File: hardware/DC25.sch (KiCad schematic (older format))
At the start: 18 parts, among them P2 CONN_01X04, SW1 SW_DPDT_x2, U1 ATMEGA328P-AU, Y1 16MHz

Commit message: Some progress
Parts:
- DIS1: footprint footprints:VFD -> (none)
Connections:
- net DB0: now also U1.14 ((PCINT2/OC1B/~SS~)PB2); no longer U1.1 ((PCINT19/OC2B/INT1)PD3)
- net DB1: now also U1.13 ((PCINT1/OC1A)PB1); no longer U1.2 ((PCINT20/XCK/T0)PD4)
- net DB2: now also U1.12 ((PCINT0/CLKO/ICP1)PB0); no longer U1.9 ((PCINT21/OC0B/T1)PD5)
- net DB3: now also U1.11 ((PCINT23/AIN1)PD7); no longer U1.10 ((PCINT22/OC0A/AIN0)PD6)
- net DB4: now also U1.10 ((PCINT22/OC0A/AIN0)PD6); no longer U1.11 ((PCINT23/AIN1)PD7)
- net DB5: now also U1.9 ((PCINT21/OC0B/T1)PD5); no longer U1.12 ((PCINT0/CLKO/ICP1)PB0)
- net DB6: now also U1.2 ((PCINT20/XCK/T0)PD4); no longer U1.13 ((PCINT1/OC1A)PB1)
- net DB7: now also U1.1 ((PCINT19/OC2B/INT1)PD3); no longer U1.14 ((PCINT2/OC1B/~SS~)PB2)
- net E: now also U1.23 ((PCINT8/ADC0)PC0); no longer U1.32 ((PCINT18/INT0)PD2)
- net RGB1: now also U1.30 ((PCINT16/RXD)PD0); no longer U1.23 ((PCINT8/ADC0)PC0)
- net RS: now also U1.25 ((PCINT10/ADC2)PC2); no longer U1.30 ((PCINT16/RXD)PD0)
- net RW: now also U1.24 ((PCINT9/ADC1)PC1); no longer U1.31 ((PCINT17/TXD)PD1)
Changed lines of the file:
@@
 	-1   0    0    1
-$EndComp
-$Comp
-L VFD DIS1
-U 1 1 58C89F6D
-P 3950 850
-F 0 "DIS1" H 4450 900 60  0000 C CNN
-F 1 "VFD" H 3400 900 60  0000 C CNN
-F 2 "footprints:VFD" H 3500 950 60  0001 C CNN
-F 3 "" H 3500 950 60  0001 C CNN
-	1    3950 850
-	1    0    0    -1
 $EndComp
 NoConn ~ 3500 1250
@@
 Text Label 4600 1250 3    60   ~ 0
 DB7
-Text Label 2850 2400 0    60   ~ 0
+Text Label 2850 1850 0    60   ~ 0
 RS
-Text Label 2850 2500 0    60   ~ 0
+Text Label 2850 1750 0    60   ~ 0
 RW
+Text Label 2850 1000 0    60   ~ 0
+DB0
+Text Label 2850 900  0    60   ~ 0
+DB1
+Text Label 2850 800  0    60   ~ 0
+DB2
+Text Label 2850 3100 0    60   ~ 0
+DB3
+Text Label 2850 3000 0    60   ~ 0
+DB4
+Text Label 2850 2900 0    60   ~ 0
+DB5
+Text Label 2850 2800 0    60   ~ 0
+DB6
 Text Label 2850 2700 0    60   ~ 0
-DB0
-Text Label 2850 2800 0    60   ~ 0
-DB1
-Text Label 2850 2900 0    60   ~ 0
-DB2
-Text Label 2850 3000 0    60   ~ 0
-DB3
-Text Label 2850 3100 0    60   ~ 0
-DB4
-Text Label 2850 800  0    60   ~ 0
-DB5
-Text Label 2850 900  0    60   ~ 0
-DB6
-Text Label 2850 1000 0    60   ~ 0
 DB7
 $Comp
@@
 Text Label 10300 5100 0    60   ~ 0
 RGB1
-Text Label 2850 1650 0    60   ~ 0
+Text Label 2850 2400 0    60   ~ 0
 RGB1
-NoConn ~ 2850 1750
-NoConn ~ 2850 1850
+NoConn ~ 2850 2500
+NoConn ~ 2850 2500
 NoConn ~ 2850 1950
 NoConn ~ 2850 2050
@@
 Wire Wire Line
 	850  3000 950  3000
-Text Label 2850 2600 0    60   ~ 0
+Text Label 2850 1650 0    60   ~ 0
 E
 NoConn ~ 2850 2150
@@
 	950  900  800  900
 Connection ~ 800  900
+$Comp
+L VFD DIS1
+U 1 1 58D4713E
+P 3950 850
+F 0 "DIS1" H 4450 900 60  0000 C CNN
+F 1 "VFD" H 3400 900 60  0000 C CNN
+F 2 "" H 3500 950 60  0001 C CNN
+F 3 "" H 3500 950 60  0001 C CNN
+	1    3950 850
+	1    0    0    -1
+$EndComp
 $EndSCHEMATC

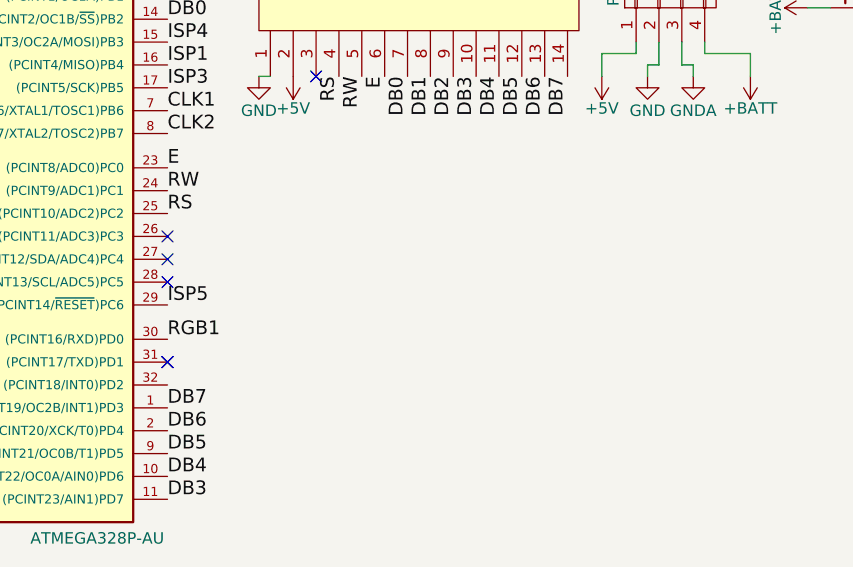
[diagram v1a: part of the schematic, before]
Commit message: Finish board layout.
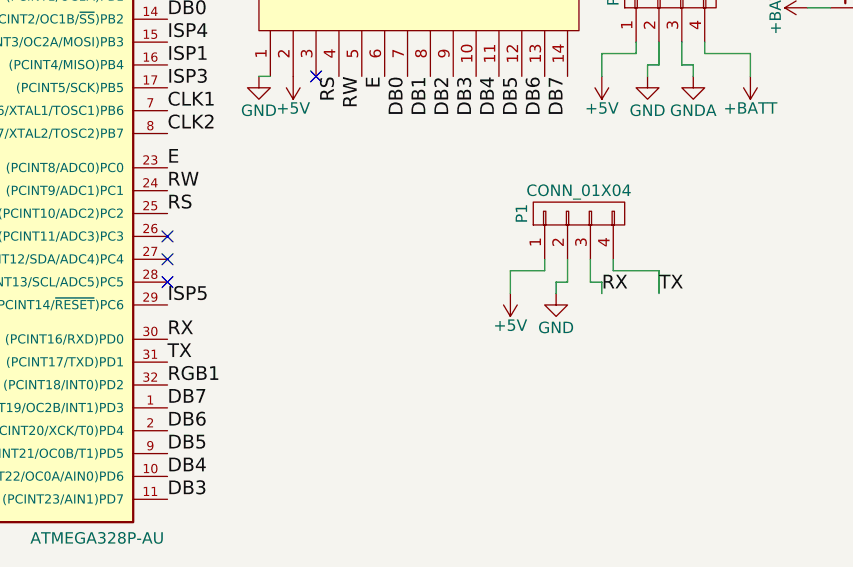
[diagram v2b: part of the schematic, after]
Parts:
- added P1: CONN_01X04, Pin_Headers:Pin_Header_Straight_1x04_Pitch2.54mm, symbol CONN_01X04
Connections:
- net +5V: now also P1.1 (P1)
- net GND: now also P1.2 (P2)
- net RGB1: now also U1.32 ((PCINT18/INT0)PD2); no longer U1.30 ((PCINT16/RXD)PD0)
- net TX: now reaches U1.31 ((PCINT17/TXD)PD1)
- net TX: now also P1.4 (P4)
- new net RX: P1.3 (P3), U1.30 ((PCINT16/RXD)PD0)
- no-connect marks 10 -> 8
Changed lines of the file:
@@
 Text Label 10300 5100 0    60   ~ 0
 RGB1
-Text Label 2850 2400 0    60   ~ 0
+Text Label 2850 2600 0    60   ~ 0
 RGB1
-NoConn ~ 2850 2500
-NoConn ~ 2850 2500
 NoConn ~ 2850 1950
 NoConn ~ 2850 2050
@@
 	1    0    0    -1
 $EndComp
+Text Label 2850 2400 0    60   ~ 0
+RX
+Text Label 2850 2500 0    60   ~ 0
+TX
+$Comp
+L CONN_01X04 P1
+U 1 1 58D6E005
+P 4650 1850
+F 0 "P1" H 4650 2100 50  0000 C CNN
+F 1 "CONN_01X04" V 4750 1850 50  0000 C CNN
+F 2 "Pin_Headers:Pin_Header_Straight_1x04_Pitch2.54mm" H 4650 1850 50  0001 C CNN
+F 3 "" H 4650 1850 50  0000 C CNN
+	1    4650 1850
+	0    -1   -1   0
+$EndComp
+$Comp
+L +5V #PWR?
+U 1 1 58D6E00B
+P 4350 2200
+F 0 "#PWR?" H 4350 2050 50  0001 C CNN
+F 1 "+5V" H 4350 2340 50  0000 C CNN
+F 2 "" H 4350 2200 50  0000 C CNN
+F 3 "" H 4350 2200 50  0000 C CNN
+	1    4350 2200
+	-1   0    0    1
+$EndComp
+$Comp
+L GND #PWR?
+U 1 1 58D6E011
+P 4550 2200
+F 0 "#PWR?" H 4550 1950 50  0001 C CNN
+F 1 "GND" H 4550 2050 50  0000 C CNN
+F 2 "" H 4550 2200 50  0000 C CNN
+F 3 "" H 4550 2200 50  0000 C CNN
+	1    4550 2200
+	1    0    0    -1
+$EndComp
+Wire Wire Line
+	4750 2200 4750 2150
+Wire Wire Line
+	4750 2150 4700 2150
+Wire Wire Line
+	4700 2150 4700 2050
+Wire Wire Line
+	4550 2200 4550 2150
+Wire Wire Line
+	4550 2150 4600 2150
+Wire Wire Line
+	4600 2150 4600 2050
+Wire Wire Line
+	4500 2050 4500 2100
+Wire Wire Line
+	4500 2100 4350 2100
+Wire Wire Line
+	4350 2100 4350 2200
+Wire Wire Line
+	4800 2050 4800 2100
+Wire Wire Line
+	4800 2100 5000 2100
+Wire Wire Line
+	5000 2100 5000 2200
+Text Label 5000 2200 0    60   ~ 0
+TX
+Text Label 4750 2200 0    60   ~ 0
+RX
 $EndSCHEMATC

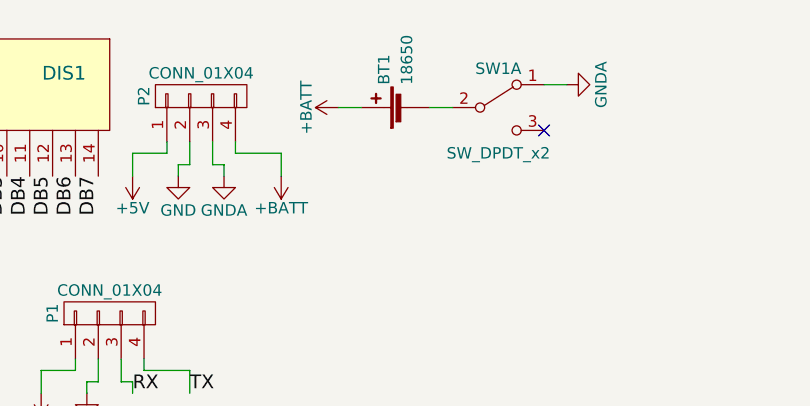
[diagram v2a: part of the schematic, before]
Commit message: remove ground via, put swith on battery positive sideq
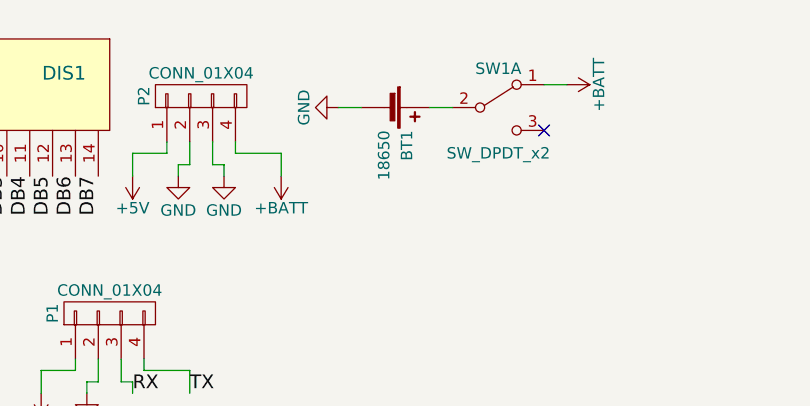
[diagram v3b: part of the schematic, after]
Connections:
- net +BATT: now also SW1.1 (A); no longer BT1.1 (+)
- net GND: now also BT1.2 (-), P2.3 (P3)
- net at SW1.2 (B): now also BT1.1 (+); no longer BT1.2 (-)
- removed net GNDA: P2.3 (P3), SW1.1 (A)
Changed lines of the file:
@@
 L +BATT #PWR011
 U 1 1 58C983F1
-P 5650 950
-F 0 "#PWR011" H 5650 800 50  0001 C CNN
-F 1 "+BATT" H 5650 1090 50  0000 C CNN
-F 2 "" H 5650 950 50  0000 C CNN
-F 3 "" H 5650 950 50  0000 C CNN
-	1    5650 950
-	0    -1   -1   0
+P 6650 850
+F 0 "#PWR011" H 6650 700 50  0001 C CNN
+F 1 "+BATT" H 6650 990 50  0000 C CNN
+F 2 "" H 6650 850 50  0000 C CNN
+F 3 "" H 6650 850 50  0000 C CNN
+	1    6650 850
+	0    1    1    0
 $EndComp
 $Comp
@@
 	-1   0    0    1
 $EndComp
-$Comp
-L GNDA #PWR013
-U 1 1 58C9851F
-P 5150 1250
-F 0 "#PWR013" H 5150 1000 50  0001 C CNN
-F 1 "GNDA" H 5150 1100 50  0000 C CNN
-F 2 "" H 5150 1250 50  0000 C CNN
-F 3 "" H 5150 1250 50  0000 C CNN
-	1    5150 1250
-	1    0    0    -1
-$EndComp
-$Comp
-L GNDA #PWR014
-U 1 1 58C985CF
-P 6650 850
-F 0 "#PWR014" H 6650 600 50  0001 C CNN
-F 1 "GNDA" H 6650 700 50  0000 C CNN
-F 2 "" H 6650 850 50  0000 C CNN
-F 3 "" H 6650 850 50  0000 C CNN
-	1    6650 850
-	0    -1   -1   0
-$EndComp
 Wire Wire Line
 	6050 950  6150 950
@@
 L Battery_Cell BT1
 U 1 1 58C995B5
-P 5950 950
-F 0 "BT1" H 6050 1050 50  0000 L CNN
-F 1 "18650" H 6050 950 50  0000 L CNN
-F 2 "Pin_Headers:Pin_Header_Straight_1x02_Pitch2.54mm" V 5950 1010 50  0001 C CNN
-F 3 "" V 5950 1010 50  0001 C CNN
-	1    5950 950
-	0    -1   -1   0
+P 5850 950
+F 0 "BT1" H 5950 1050 50  0000 L CNN
+F 1 "18650" H 5950 950 50  0000 L CNN
+F 2 "Pin_Headers:Pin_Header_Straight_1x02_Pitch2.54mm" V 5850 1010 50  0001 C CNN
+F 3 "" V 5850 1010 50  0001 C CNN
+	1    5850 950
+	0    1    1    0
 $EndComp
 Wire Wire Line
@@
 $EndComp
 $Comp
-L +5V #PWR?
+L +5V #PWR017
 U 1 1 58D6E00B
 P 4350 2200
-F 0 "#PWR?" H 4350 2050 50  0001 C CNN
+F 0 "#PWR017" H 4350 2050 50  0001 C CNN
 F 1 "+5V" H 4350 2340 50  0000 C CNN
 F 2 "" H 4350 2200 50  0000 C CNN
@@
 $EndComp
 $Comp
-L GND #PWR?
+L GND #PWR018
 U 1 1 58D6E011
 P 4550 2200
-F 0 "#PWR?" H 4550 1950 50  0001 C CNN
+F 0 "#PWR018" H 4550 1950 50  0001 C CNN
 F 1 "GND" H 4550 2050 50  0000 C CNN
 F 2 "" H 4550 2200 50  0000 C CNN
@@
 Text Label 4750 2200 0    60   ~ 0
 RX
+$Comp
+L GND #PWR?
+U 1 1 58D71D3F
+P 5150 1250
+F 0 "#PWR?" H 5150 1000 50  0001 C CNN
+F 1 "GND" H 5150 1100 50  0000 C CNN
+F 2 "" H 5150 1250 50  0000 C CNN
+F 3 "" H 5150 1250 50  0000 C CNN
+	1    5150 1250
+	1    0    0    -1
+$EndComp
+$Comp
+L GND #PWR?
+U 1 1 58D71D83
+P 5650 950
+F 0 "#PWR?" H 5650 700 50  0001 C CNN
+F 1 "GND" H 5650 800 50  0000 C CNN
+F 2 "" H 5650 950 50  0000 C CNN
+F 3 "" H 5650 950 50  0000 C CNN
+	1    5650 950
+	0    1    1    0
+$EndComp
 $EndSCHEMATC
